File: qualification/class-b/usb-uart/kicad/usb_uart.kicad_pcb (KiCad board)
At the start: 4 copper layers, 45 x 39.7 mm, 36 parts, among them J1 TYPE-C-31-M-12, J2 UART1, J3 FLOW1, J4 RS485, U1 CH342F, U2 LDO, U3 THVD1450D

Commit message: SYN-66 - Align the header row and re-route
The four bottom headers were pinned in one row at y 33.4, but a rotated
1x3 header courtyard is 8.62 mm long and the sidecar put J3 only 8.1 mm
from J4. The placer could not move J4, which is also a hard override, so
it parked J3 at (22.56, 37.4), one row below.

Space the row at 9.1 mm and pin J_VIO, J2, J3 and J4 together at y 37.4,
flush on the bottom edge. Re-route with FreeRouting 2.4.1 through the MCP
export:

- release_ready true, 0 open nets, 0 unconnected items
- 253 track segments, 42 vias, 565.1 mm of copper
- kicad-cli DRC: 0 errors, 42 warnings
- kicad-cli ERC: 1 error (VIO power_pin_not_driven), 119 warnings
- signal integrity: 23 warnings, none blocking
- board 45.0 x 39.73 mm

Refresh the KiCad files, reports, images and SHA256SUMS.

Signed-off-by: nyagamunene <stevenyaga2014@gmail.com>
Co-authored-by: CommandCodeBot <noreply@commandcode.ai>
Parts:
- moved J2 4.12 mm to (13.9, 37.4)
- moved J_VIO 4.12 mm to (4.82, 37.4)
- moved J4 4.00 mm to (32.1, 37.4)
- moved J3 3.00 mm to (23.0, 37.4)
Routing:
- net VIO: track 59.8 -> 80.1 mm, vias 2 -> 0
- net TXD1: track 37.2 -> 29.5 mm
- net RTS1: track 26.1 -> 19.1 mm, vias 1 -> 0
- net RXD1: track 6.36 -> 10.8 mm
- net +3V3: track 21.2 -> 25.6 mm
- net RS485_A: track 19.9 -> 23.3 mm
- net CC2: track 10.7 -> 13.5 mm, vias 0 -> 2
- net USB_DP: track 14.4 -> 17.1 mm, vias 2 -> 0
- net MODEM_IDLE: track 43.2 -> 40.9 mm
- net RS485_B: track 32.0 -> 33.7 mm, vias 0 -> 1
- net CTS1: track 11.6 -> 10.3 mm
- net CTS0_LOW: track 23.4 -> 24.5 mm
- net DTR1: track 24.1 -> 23.1 mm
- net VBUS: track 86.7 -> 87.6 mm, vias 1 -> 2
- net TNOW0: track 35.4 -> 34.5 mm, vias 2 -> 3
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
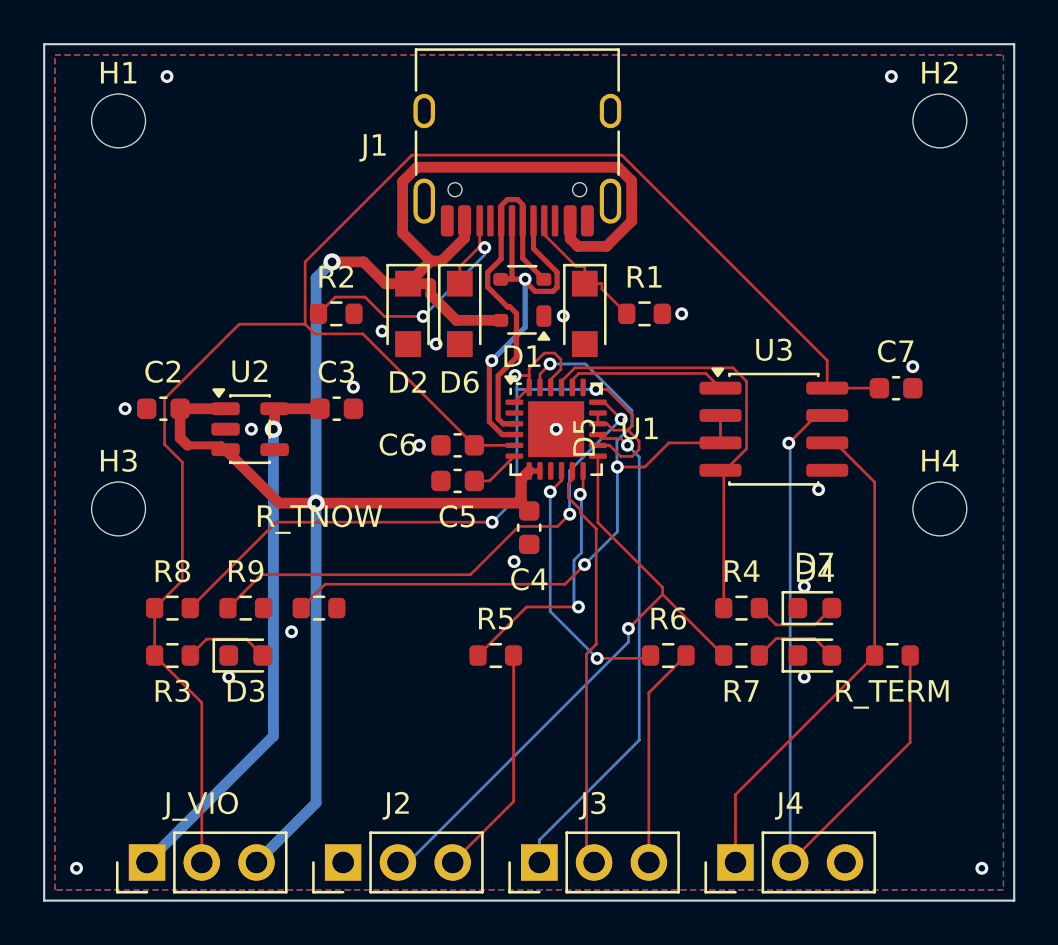
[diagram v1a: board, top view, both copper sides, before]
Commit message: Compact the USB-UART board to 41.5 x 32.23 mm
Pull the mounting holes in, move the bottom parts and header row up,
fill the top corners, and re-route. The board is 7.5 mm shorter than
the previously committed outline.

Drop isolated ground-zone islands in the exporter, and treat a zone
KiCad lists against itself as a fill warning instead of an open net.
Add sidecar label overrides for D7, R7 and R_TERM.

FreeRouting: release_ready true, 0 open nets, 0 unconnected, 255
segments, 44 vias, 471.9 mm of copper.

Co-authored-by: CommandCodeBot <noreply@commandcode.ai>
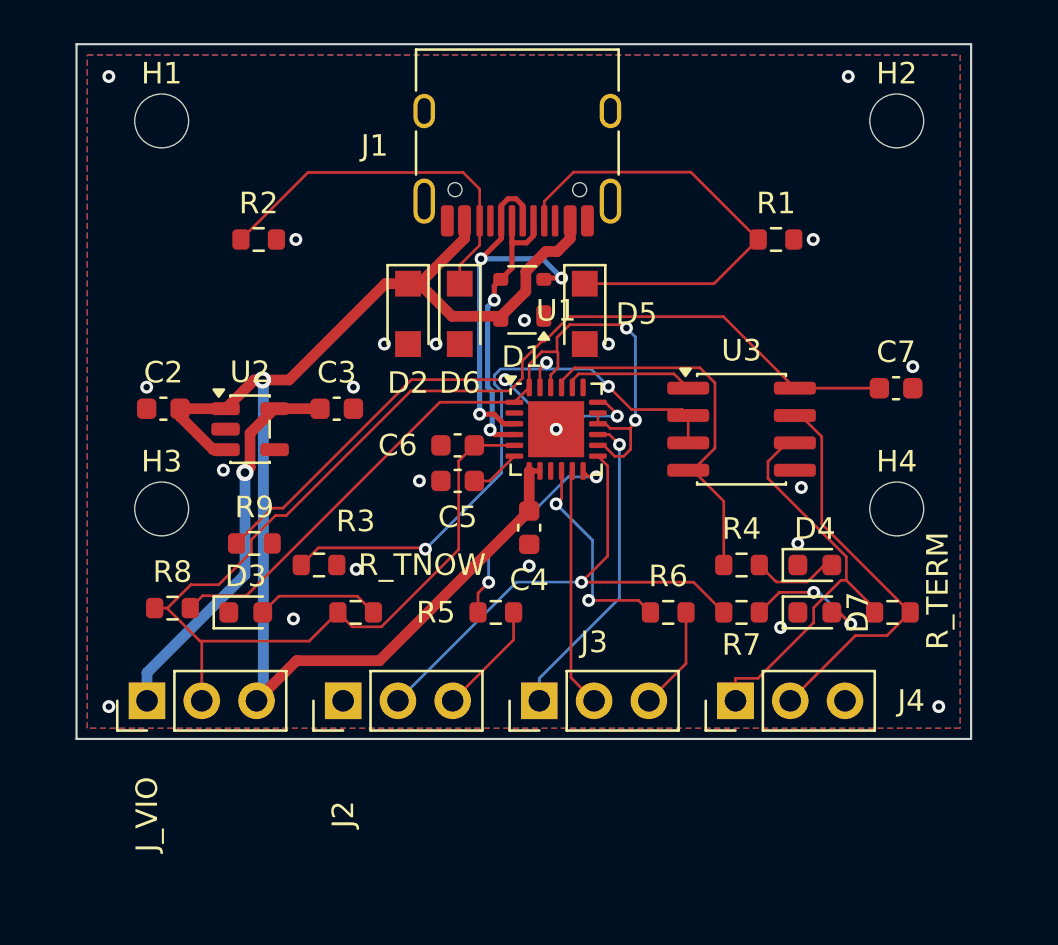
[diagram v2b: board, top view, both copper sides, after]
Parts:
- moved R3 8.73 mm to (14.5, 25.8)
- moved J2 7.50 mm to (13.9, 29.9)
- moved J3 7.50 mm to (23.0, 29.9)
- moved J4 7.50 mm to (32.1, 29.9)
- moved J_VIO 7.50 mm to (4.82, 29.9)
- moved R1 7.01 mm to (34.0, 8.50)
- moved R2 4.99 mm to (10.0, 8.50)
- moved R9 3.03 mm to (9.80, 22.6)
- moved D3 2.00 mm to (9.40, 25.8)
- moved D4 2.00 mm to (35.8, 23.6)
- moved D7 2.00 mm to (35.8, 25.8)
- moved H1 2.00 mm to (5.50, 3.00)
- moved H2 2.00 mm to (39.6, 3.00)
- moved H3 2.00 mm to (5.50, 21.0)
- moved H4 2.00 mm to (39.6, 21.0)
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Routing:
- net VBUS: track 87.6 -> 64.7 mm, vias 2 -> 1
- net CC1: track 6.60 -> 21.6 mm
- net RS485_B: track 33.7 -> 18.8 mm, vias 1 -> 0
- net VIO: track 80.1 -> 67.6 mm
- net DTR1: track 23.1 -> 14.6 mm
- net RTS1: track 19.1 -> 11.1 mm
- net +3V3: track 25.6 -> 18.1 mm
- net TNOW0: track 34.5 -> 28.6 mm
- net RXD1: track 10.8 -> 5.27 mm
- net CTS1: track 10.3 -> 4.81 mm
- net TXD1: track 29.5 -> 24.5 mm
- net USB_DN: track 17.9 -> 13.3 mm
- net RS485_A: track 23.3 -> 19.1 mm
- net CC2: track 13.5 -> 17.5 mm, vias 2 -> 0
- net TXD0: track 20.6 -> 17.6 mm
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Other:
- board size 45 x 39.7 mm -> 41.5 x 32.2 mm

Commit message: SYN-66 - Make the board two layers and re-route
The four-layer board carried no routing on In1.Cu or In2.Cu: all 255
segments were on F.Cu (214) and B.Cu (41), and both inner layers were
GND pours only. Drop them.

- `layers 2`, no stackup block; the exporter writes the 1.6 mm default.
- The USB pair loses its 90 ohm target: at 1.6 mm on two layers the
  estimate needs about 1.18 mm traces, and the routing gate rejects the
  0.242 mm pair as 65 percent off. The netclass width stays.
- At J3's old x 25.56 FreeRouting left DTR1 (U1 pin 15 to J3 pin 1)
  unrouted. Move J3 to 27.0 and J4 to 36.1 to keep the 8.62 mm header
  courtyards apart.
- FreeRouting 2.4.1: release_ready true, 0 open nets, 271 track
  segments, 38 vias, 507.7 mm of copper.
- kicad-cli DRC: 0 errors, 39 warnings, one self-referential zone item.
- kicad-cli ERC: 1 error (VIO power_pin_not_driven), 119 warnings.
- Signal integrity: 15 warnings, none blocking; all are layer changes
  with no ground return via within 1.53 mm.

Refresh the KiCad files, reports, images and SHA256SUMS.

Co-authored-by: CommandCodeBot <noreply@commandcode.ai>
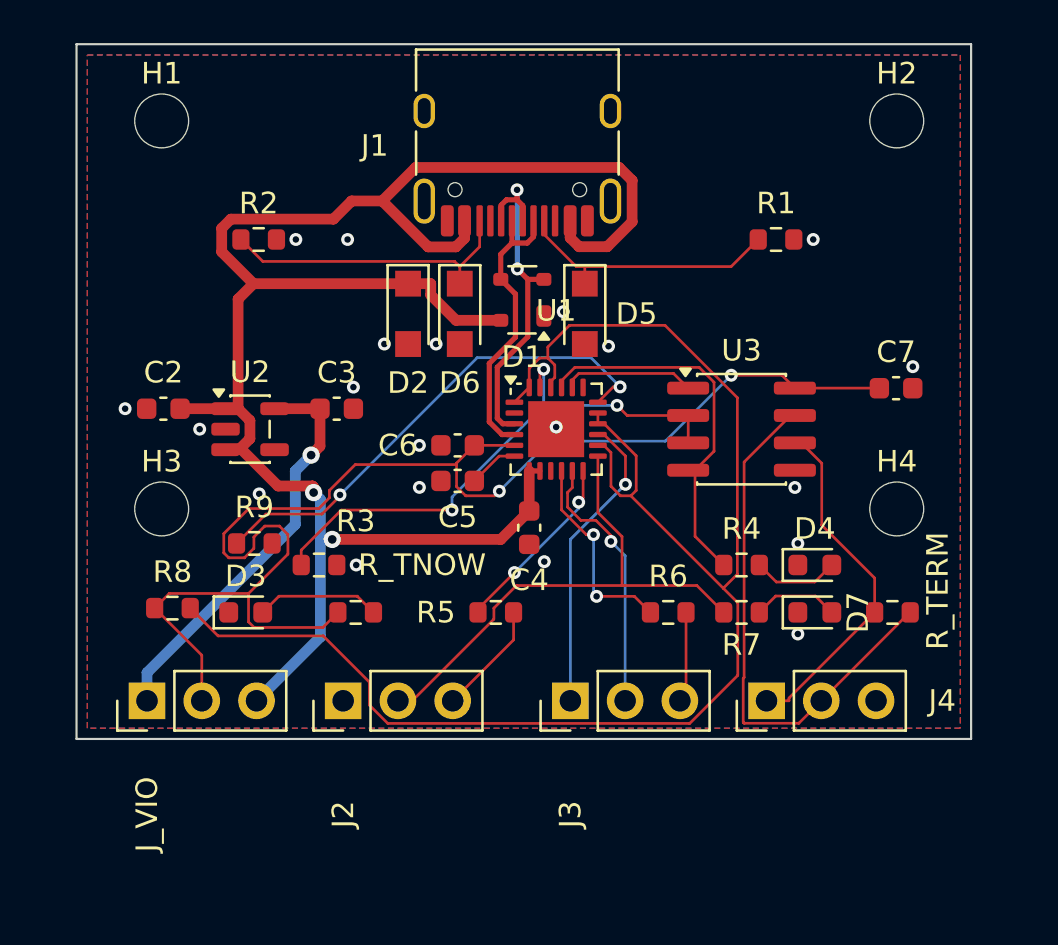
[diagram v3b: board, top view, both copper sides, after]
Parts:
- moved J4 1.44 mm to (33.6, 29.9)
- moved J3 1.44 mm to (24.5, 29.9)
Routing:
- net MODEM_IDLE: track 38.4 -> 72.5 mm, vias 2 -> 0
- net VBUS: track 64.7 -> 87.8 mm, vias 1 -> 2
- net CC1: track 21.6 -> 12.5 mm
- net RS485_B: track 18.8 -> 25.2 mm
- net VIO: track 67.6 -> 63.0 mm, vias 0 -> 2
- net CC2: track 17.5 -> 14.0 mm
- net TNOW0: track 28.6 -> 25.8 mm
- net RS485_A: track 19.1 -> 16.4 mm
- net USB_DP: track 18.8 -> 16.2 mm, vias 3 -> 2
- net LED_TX1: track 6.33 -> 3.99 mm, vias 2 -> 0
- net RXD1_MCU: track 10.1 -> 8.58 mm
- net RTS1: track 11.1 -> 12.3 mm, vias 0 -> 1
- net +3V3: track 18.1 -> 19.0 mm
- net CTS1: track 4.81 -> 4.22 mm
- net CTS0_LOW: track 22.7 -> 23.3 mm
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- removed copper zone on In1.Cu, net GND
- removed copper zone on In2.Cu, net GND
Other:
- copper layers 4 -> 2

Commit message: SYN-66 - Re-export and re-route the board with the TX LED fix and clean silkscreen
Signed-off-by: nyagamunene <stevenyaga2014@gmail.com>
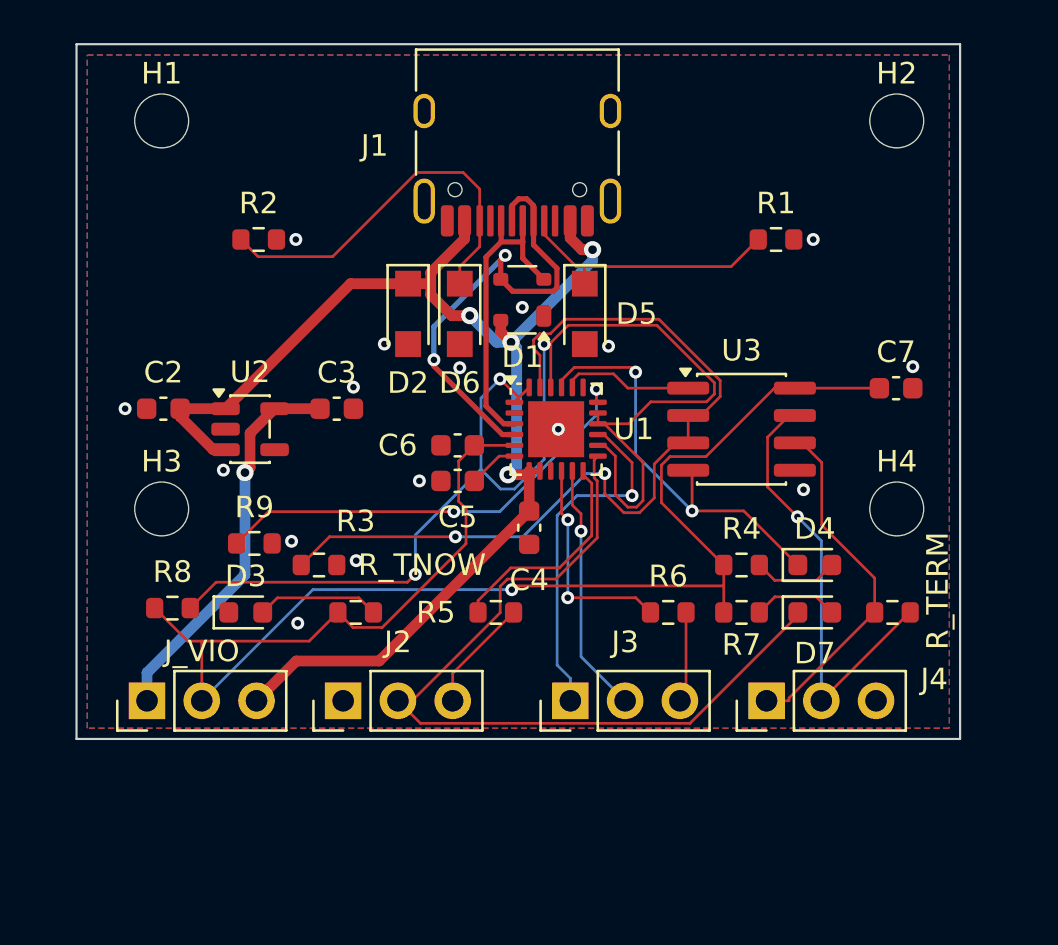
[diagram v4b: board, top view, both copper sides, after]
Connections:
- D4 pad 1: GND -> TXD0
- D7 pad 1: GND -> TXD1
- R4 pad 1: TXD0 -> VIO
- R7 pad 1: TXD1 -> VIO
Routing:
- net VBUS: track 87.8 -> 61.0 mm, vias 2 -> 4
- net TNOW0: track 25.8 -> 39.7 mm, vias 3 -> 2
- net TXD1: track 24.6 -> 38.2 mm
- net MODEM_IDLE: track 72.5 -> 60.7 mm, vias 0 -> 3
- net VIO: track 63.0 -> 73.2 mm, vias 2 -> 1
- net USB_DN: track 13.6 -> 21.9 mm, vias 0 -> 2
- net RS485_B: track 25.2 -> 20.8 mm, vias 0 -> 1
- net CC2: track 14.0 -> 18.1 mm
- net CTS0_LOW: track 23.3 -> 21.0 mm
- net DTR1: track 14.1 -> 16.4 mm
- net TXD0: track 17.6 -> 19.5 mm, vias 0 -> 2
- net RXD1_MCU: track 8.58 -> 10.2 mm, vias 2 -> 0
- net USB_DP: track 16.2 -> 14.7 mm, vias 2 -> 0
- net +3V3: track 19.0 -> 18.1 mm
- net CTS1_MCU: track 9.49 -> 10.1 mm
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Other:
- board size 41.5 x 32.2 mm -> 41 x 32.2 mm

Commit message: SYN-66 - Move J3 and J4 1 mm left so the GND pour is connected, regenerate the board
Signed-off-by: nyagamunene <stevenyaga2014@gmail.com>
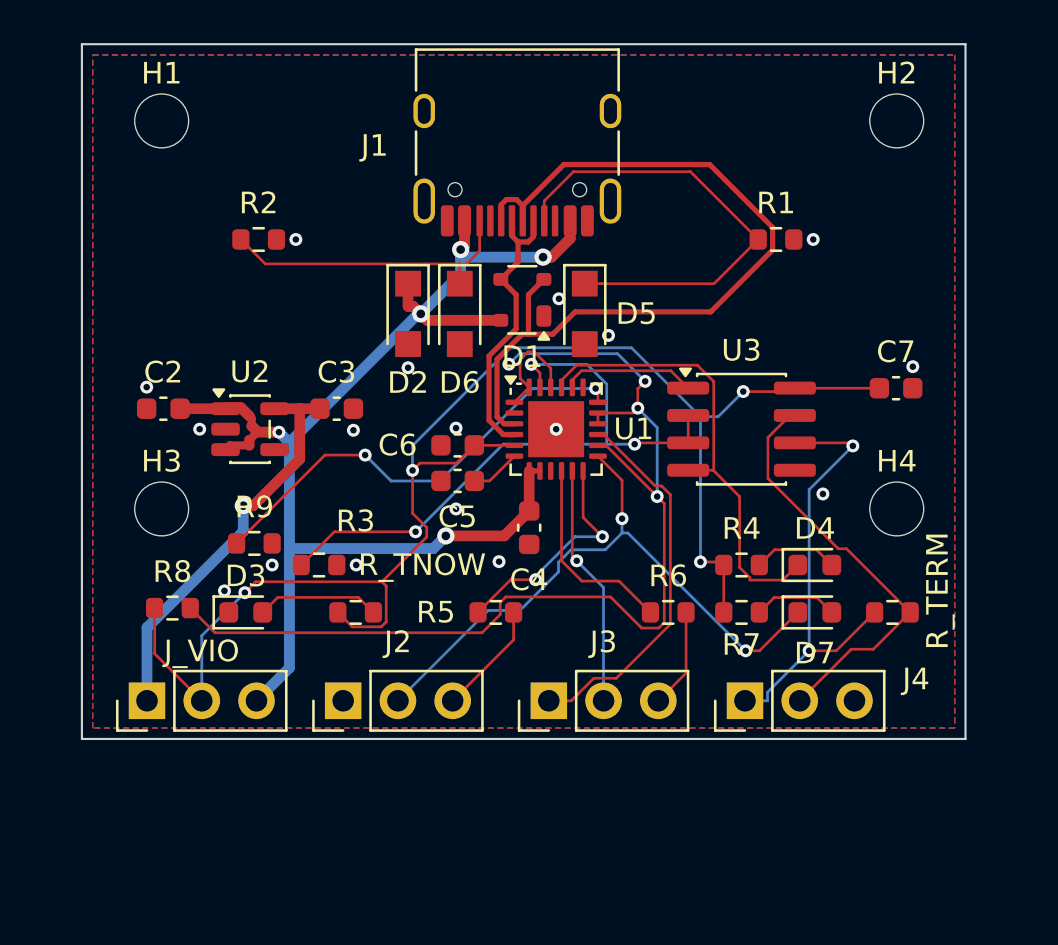
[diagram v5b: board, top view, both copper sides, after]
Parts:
- moved J3 1.00 mm to (23.5, 29.9)
- moved J4 1.00 mm to (32.6, 29.9)
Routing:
- net USB_DP: track 14.7 -> 38.6 mm
- net TNOW0: track 39.7 -> 29.5 mm, vias 2 -> 3
- net TXD1: track 38.2 -> 29.1 mm, vias 0 -> 2
- net CC1: track 12.5 -> 21.6 mm
- net USB_DN: track 21.9 -> 13.5 mm, vias 2 -> 0
- net MODEM_IDLE: track 60.7 -> 55.0 mm, vias 3 -> 4
- net RS485_A: track 16.4 -> 21.0 mm, vias 0 -> 2
- net CC2: track 18.1 -> 14.1 mm
- net VIO: track 73.2 -> 70.3 mm, vias 1 -> 4
- net TXD0: track 19.5 -> 21.6 mm, vias 2 -> 0
- net DTR1: track 16.4 -> 17.6 mm, vias 1 -> 0
- net RS485_B: track 20.8 -> 19.6 mm, vias 1 -> 0
- net CTS1_MCU: track 10.1 -> 9.28 mm, vias 2 -> 0
- net +3V3: track 18.1 -> 18.9 mm
- net VBUS: track 61.0 -> 60.4 mm, vias 4 -> 5
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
